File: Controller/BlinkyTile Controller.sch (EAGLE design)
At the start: 26 parts, among them CON1 USB_MICROSMT+THRUHULE, CON2 F-2X04-DIL-100, Q1 CRYSTAL_4PAD2520, SW1 SPST_TACT-EVQQ2, SW2 SPST_TACT-EVQQ2, U1 MK20D--VFM5, U2 W25Q80BV, U3 74LVC1G17DCK, U4 74LVC1G17DCK, U5 74LVC1G17DCK

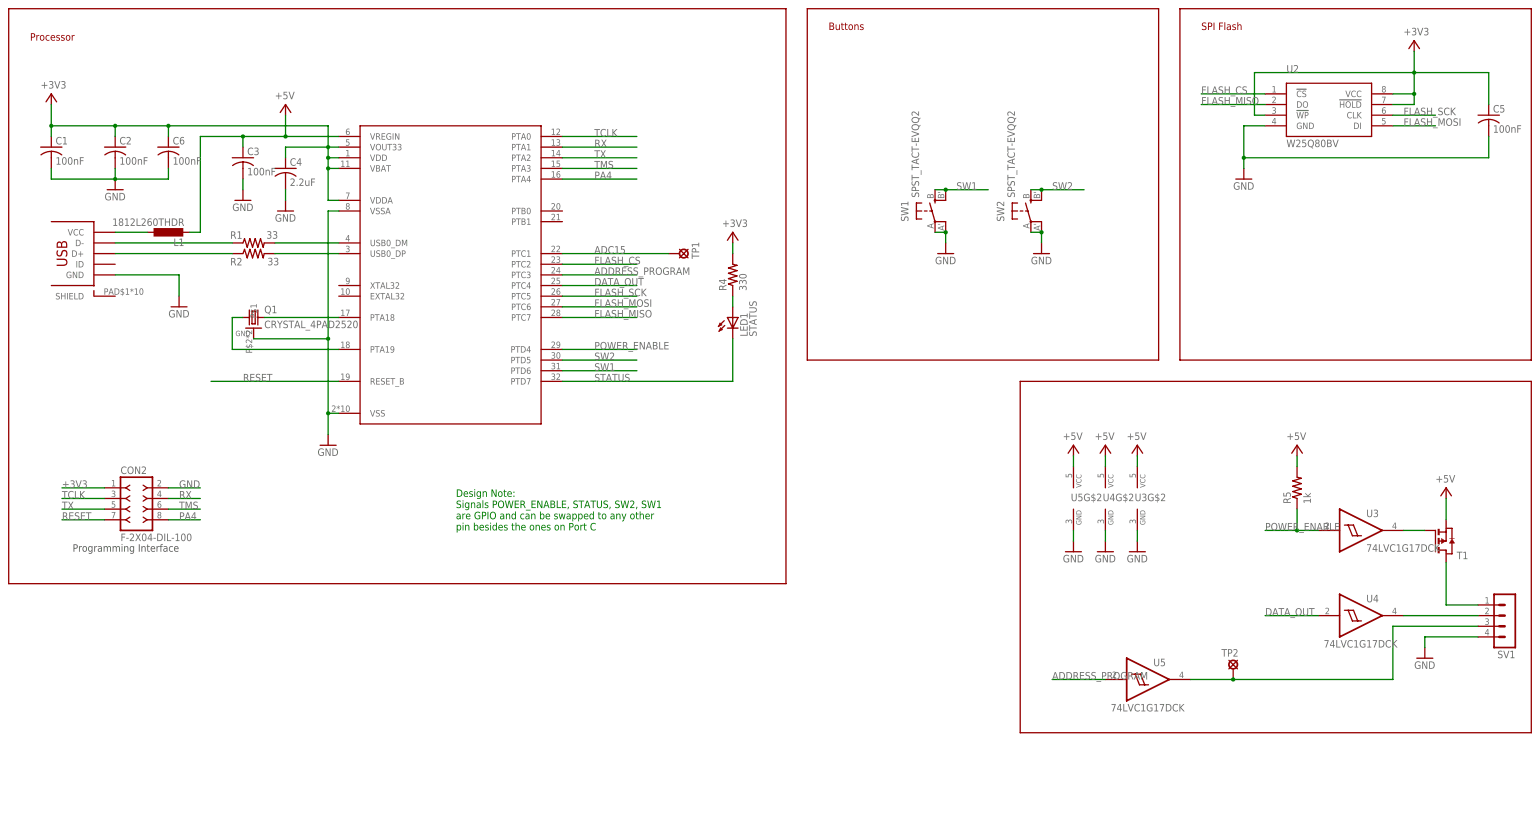
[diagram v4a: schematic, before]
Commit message: Updated controller and panel designs
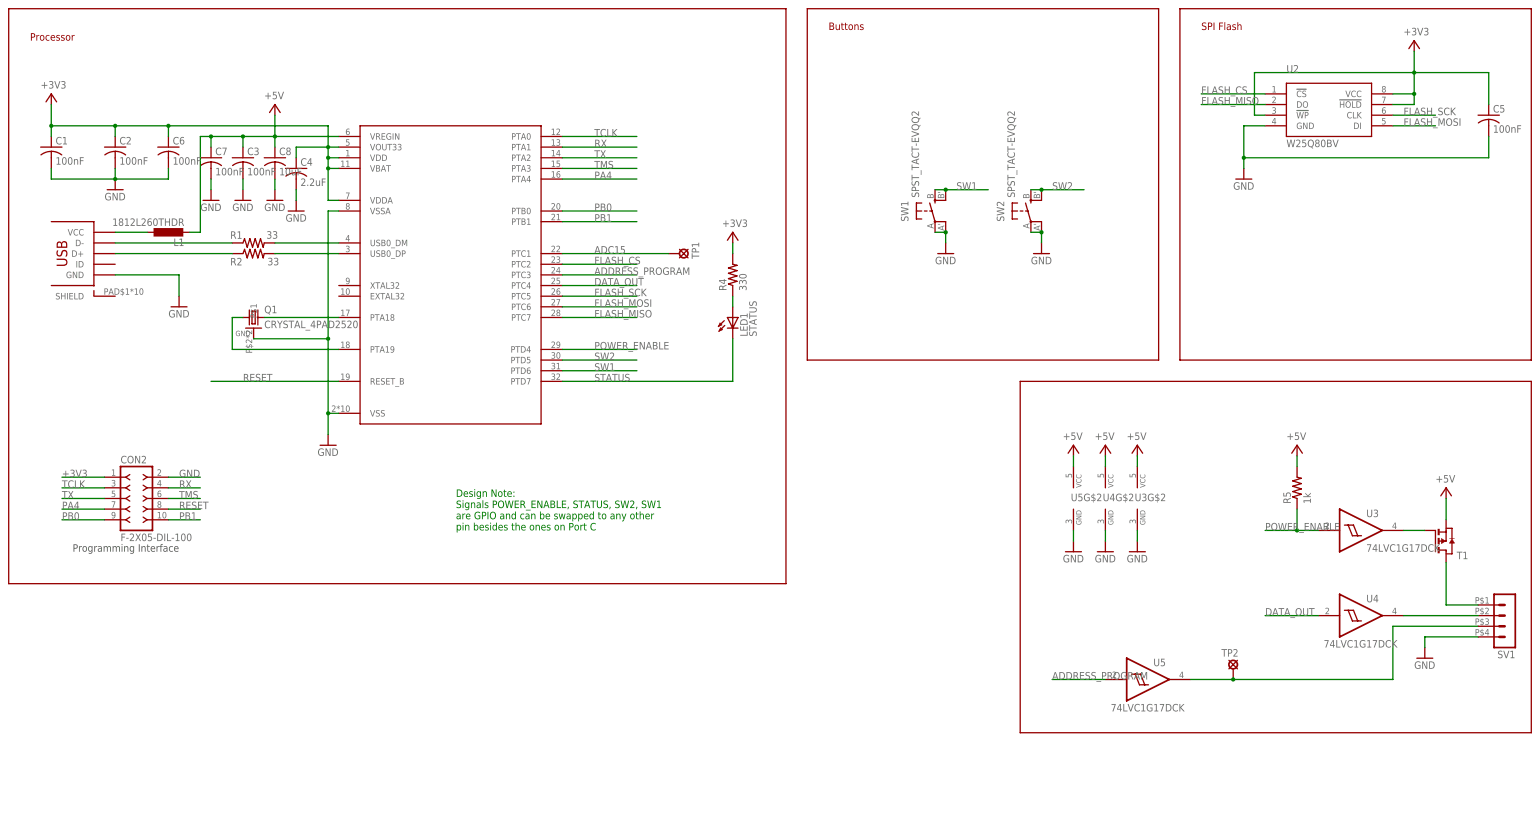
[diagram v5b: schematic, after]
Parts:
- added C7: 100nF, adafruit:C-USC0402
- added C8: 10uF, adafruit:C-USC0805K
- CON2: value F-2X04-DIL-100 -> F-2X05-DIL-100; device con-headers-jp:F-2X04-DIL-100 -> con-headers-jp:F-2X05-DIL-100
- SV1: device con-lstb:MA04-1 -> dodocohedreled:4-PIN_DUPONT
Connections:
- new net PB0: CON2.9, U1.PTB0
- new net PB1: CON2.10, U1.PTB1
- net +5V: now also C7.1, C8.1
- net GND: now also C7.2, C8.2
- net PA4: now also CON2.7; no longer CON2.8
- net RESET: now also CON2.8; no longer CON2.7
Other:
- moved on the sheet: C4, SV1
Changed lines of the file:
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@@
 <part name="TP2" library="solpad" deviceset="SE11" device="" value="ADDRESS"/>
 <part name="TP1" library="solpad" deviceset="SE11" device="" value="ADCIN"/>
-<part name="CON2" library="con-headers-jp" deviceset="F-2X04-" device="DIL-100" value="F-2X04-DIL-100"/>
+<part name="CON2" library="con-headers-jp" deviceset="F-2X05-" device="DIL-100" value="F-2X05-DIL-100"/>
 <part name="U3" library="74xx-little-us" deviceset="74*1G17" device="DCK" technology="LVC"/>
 <part name="T1" library="zetex" deviceset="PMOSSOT23" device=""/>
@@
 <part name="C6" library="adafruit" deviceset="C-US" device="C0402" value="100nF"/>
 <part name="R5" library="adafruit" deviceset="R-US_" device="R0402" value="1k"/>
+<part name="SV1" library="dodocohedreled" deviceset="4-PIN_DUPONT" device=""/>
 <part name="P+5" library="supply1" deviceset="+5V" device=""/>
-<part name="SV1" library="con-lstb" deviceset="MA04-1" device=""/>
+<part name="C7" library="adafruit" deviceset="C-US" device="C0402" value="100nF"/>
+<part name="GND6" library="supply1" deviceset="GND" device=""/>
+<part name="C8" library="adafruit" deviceset="C-US" device="C0805K" value="10uF"/>
+<part name="GND11" library="supply1" deviceset="GND" device=""/>
 </parts>
 <sheets>
@@
 <instance part="CON1" gate="G$1" x="33.02" y="190.5"/>
 <instance part="Q1" gate="G$1" x="73.66" y="175.26"/>
-<instance part="C4" gate="G$1" x="81.28" y="210.82"/>
-<instance part="GND9" gate="1" x="81.28" y="200.66"/>
+<instance part="C4" gate="G$1" x="83.82" y="210.82"/>
+<instance part="GND9" gate="1" x="83.82" y="200.66"/>
 <instance part="GND15" gate="1" x="40.64" y="205.74"/>
 <instance part="GND10" gate="1" x="309.88" y="208.28"/>
@@
 <attribute name="VALUE" x="185.42" y="196.85" size="1.778" layer="96"/>
 </instance>
-<instance part="P+9" gate="1" x="81.28" y="226.06" smashed="yes">
-<attribute name="VALUE" x="78.74" y="227.33" size="1.778" layer="96"/>
+<instance part="P+9" gate="1" x="78.74" y="226.06" smashed="yes">
+<attribute name="VALUE" x="76.2" y="227.33" size="1.778" layer="96"/>
 </instance>
 <instance part="C3" gate="G$1" x="71.12" y="213.36"/>
@@
 <instance part="C6" gate="G$1" x="53.34" y="215.9"/>
 <instance part="R5" gate="G$1" x="322.58" y="134.62" rot="R90"/>
+<instance part="SV1" gate="1" x="373.38" y="101.6" rot="R180"/>
 <instance part="P+5" gate="1" x="322.58" y="144.78" smashed="yes">
 <attribute name="VALUE" x="320.04" y="146.05" size="1.778" layer="96"/>
 </instance>
-<instance part="SV1" gate="1" x="373.38" y="101.6" rot="R180"/>
+<instance part="C7" gate="G$1" x="63.5" y="213.36"/>
+<instance part="GND6" gate="1" x="63.5" y="203.2"/>
+<instance part="C8" gate="G$1" x="78.74" y="213.36"/>
+<instance part="GND11" gate="1" x="78.74" y="203.2"/>
 </instances>
 <busses>
@@
 <segment>
 <pinref part="C4" gate="G$1" pin="2"/>
-<wire x1="81.28" y1="205.74" x2="81.28" y2="203.2" width="0.1524" layer="91"/>
+<wire x1="83.82" y1="205.74" x2="83.82" y2="203.2" width="0.1524" layer="91"/>
 <pinref part="GND9" gate="1" pin="GND"/>
 </segment>
@@
 <segment>
 <pinref part="CON2" gate="G$1" pin="2"/>
-<wire x1="53.34" y1="134.62" x2="60.96" y2="134.62" width="0.1524" layer="91"/>
-<label x="55.88" y="134.62" size="1.778" layer="95"/>
+<wire x1="53.34" y1="137.16" x2="60.96" y2="137.16" width="0.1524" layer="91"/>
+<label x="55.88" y="137.16" size="1.778" layer="95"/>
 </segment>
 <segment>
@@
 <junction x="91.44" y="170.18"/>
 </segment>
+<segment>
+<pinref part="C7" gate="G$1" pin="2"/>
+<pinref part="GND6" gate="1" pin="GND"/>
+<wire x1="63.5" y1="208.28" x2="63.5" y2="205.74" width="0.1524" layer="91"/>
+</segment>
+<segment>
+<pinref part="C8" gate="G$1" pin="2"/>
+<pinref part="GND11" gate="1" pin="GND"/>
+<wire x1="78.74" y1="208.28" x2="78.74" y2="205.74" width="0.1524" layer="91"/>
+</segment>
 </net>
 <net name="N$2" class="0">
@@
 <wire x1="60.96" y1="195.58" x2="60.96" y2="218.44" width="0.1524" layer="91"/>
 <pinref part="U1" gate="G$1" pin="VREGIN"/>
-<wire x1="93.98" y1="218.44" x2="81.28" y2="218.44" width="0.1524" layer="91"/>
-<wire x1="81.28" y1="223.52" x2="81.28" y2="218.44" width="0.1524" layer="91"/>
-<junction x="81.28" y="218.44"/>
+<wire x1="93.98" y1="218.44" x2="78.74" y2="218.44" width="0.1524" layer="91"/>
+<wire x1="78.74" y1="223.52" x2="78.74" y2="218.44" width="0.1524" layer="91"/>
+<junction x="78.74" y="218.44"/>
 <pinref part="C3" gate="G$1" pin="1"/>
-<wire x1="71.12" y1="218.44" x2="60.96" y2="218.44" width="0.1524" layer="91"/>
+<wire x1="71.12" y1="218.44" x2="63.5" y2="218.44" width="0.1524" layer="91"/>
+<wire x1="63.5" y1="218.44" x2="60.96" y2="218.44" width="0.1524" layer="91"/>
 <wire x1="71.12" y1="218.44" x2="71.12" y2="215.9" width="0.1524" layer="91"/>
-<wire x1="81.28" y1="218.44" x2="71.12" y2="218.44" width="0.1524" layer="91"/>
+<wire x1="78.74" y1="218.44" x2="71.12" y2="218.44" width="0.1524" layer="91"/>
 <junction x="71.12" y="218.44"/>
+<pinref part="C7" gate="G$1" pin="1"/>
+<wire x1="63.5" y1="215.9" x2="63.5" y2="218.44" width="0.1524" layer="91"/>
+<junction x="63.5" y="218.44"/>
+<pinref part="C8" gate="G$1" pin="1"/>
+<wire x1="78.74" y1="215.9" x2="78.74" y2="218.44" width="0.1524" layer="91"/>
 </segment>
 <segment>
@@
 <segment>
 <pinref part="R5" gate="G$1" pin="2"/>
+<wire x1="322.58" y1="142.24" x2="322.58" y2="139.7" width="0.1524" layer="91"/>
 <pinref part="P+5" gate="1" pin="+5V"/>
-<wire x1="322.58" y1="142.24" x2="322.58" y2="139.7" width="0.1524" layer="91"/>
 </segment>
 </net>
@@
 <pinref part="U1" gate="G$1" pin="VBAT"/>
 <pinref part="C4" gate="G$1" pin="1"/>
-<wire x1="81.28" y1="215.9" x2="81.28" y2="213.36" width="0.1524" layer="91"/>
+<wire x1="83.82" y1="215.9" x2="83.82" y2="213.36" width="0.1524" layer="91"/>
 <pinref part="U1" gate="G$1" pin="VOUT33"/>
 <wire x1="93.98" y1="215.9" x2="91.44" y2="215.9" width="0.1524" layer="91"/>
-<wire x1="91.44" y1="215.9" x2="81.28" y2="215.9" width="0.1524" layer="91"/>
+<wire x1="91.44" y1="215.9" x2="83.82" y2="215.9" width="0.1524" layer="91"/>
 <wire x1="91.44" y1="215.9" x2="91.44" y2="213.36" width="0.1524" layer="91"/>
 <pinref part="U1" gate="G$1" pin="VDD"/>
@@
 <segment>
 <pinref part="CON2" gate="G$1" pin="1"/>
+<wire x1="38.1" y1="137.16" x2="27.94" y2="137.16" width="0.1524" layer="91"/>
+<label x="27.94" y="137.16" size="1.778" layer="95"/>
+</segment>
+</net>
+<net name="TCLK" class="0">
+<segment>
+<pinref part="CON2" gate="G$1" pin="3"/>
 <wire x1="38.1" y1="134.62" x2="27.94" y2="134.62" width="0.1524" layer="91"/>
 <label x="27.94" y="134.62" size="1.778" layer="95"/>
-</segment>
-</net>
-<net name="TCLK" class="0">
-<segment>
-<pinref part="CON2" gate="G$1" pin="3"/>
-<wire x1="38.1" y1="132.08" x2="27.94" y2="132.08" width="0.1524" layer="91"/>
-<label x="27.94" y="132.08" size="1.778" layer="95"/>
 </segment>
 <segment>
@@
 <segment>
 <pinref part="CON2" gate="G$1" pin="6"/>
-<wire x1="53.34" y1="129.54" x2="60.96" y2="129.54" width="0.1524" layer="91"/>
-<label x="55.88" y="129.54" size="1.778" layer="95"/>
+<wire x1="53.34" y1="132.08" x2="60.96" y2="132.08" width="0.1524" layer="91"/>
+<label x="55.88" y="132.08" size="1.778" layer="95"/>
 </segment>
 </net>
@@
 <segment>
 <pinref part="CON2" gate="G$1" pin="4"/>
-<wire x1="60.96" y1="132.08" x2="53.34" y2="132.08" width="0.1524" layer="91"/>
-<label x="55.88" y="132.08" size="1.778" layer="95"/>
+<wire x1="60.96" y1="134.62" x2="53.34" y2="134.62" width="0.1524" layer="91"/>
+<label x="55.88" y="134.62" size="1.778" layer="95"/>
 </segment>
 </net>
@@
 <segment>
 <pinref part="CON2" gate="G$1" pin="5"/>
-<wire x1="38.1" y1="129.54" x2="27.94" y2="129.54" width="0.1524" layer="91"/>
-<label x="27.94" y="129.54" size="1.778" layer="95"/>
+<wire x1="38.1" y1="132.08" x2="27.94" y2="132.08" width="0.1524" layer="91"/>
+<label x="27.94" y="132.08" size="1.778" layer="95"/>
 </segment>
 </net>
@@
 </segment>
 <segment>
-<pinref part="CON2" gate="G$1" pin="7"/>
-<wire x1="38.1" y1="127" x2="27.94" y2="127" width="0.1524" layer="91"/>
-<label x="27.94" y="127" size="1.778" layer="95"/>
+<pinref part="CON2" gate="G$1" pin="8"/>
+<wire x1="53.34" y1="129.54" x2="60.96" y2="129.54" width="0.1524" layer="91"/>
+<label x="55.88" y="129.54" size="1.778" layer="95"/>
 </segment>
 </net>
@@
 </segment>
 <segment>
-<pinref part="CON2" gate="G$1" pin="8"/>
+<pinref part="CON2" gate="G$1" pin="7"/>
+<wire x1="38.1" y1="129.54" x2="27.94" y2="129.54" width="0.1524" layer="91"/>
+<label x="27.94" y="129.54" size="1.778" layer="95"/>
+</segment>
+</net>
+<net name="PB0" class="0">
+<segment>
+<pinref part="U1" gate="G$1" pin="PTB0"/>
+<wire x1="147.32" y1="200.66" x2="165.1" y2="200.66" width="0.1524" layer="91"/>
+<label x="154.94" y="200.66" size="1.778" layer="95"/>
+</segment>
+<segment>
+<pinref part="CON2" gate="G$1" pin="9"/>
+<wire x1="38.1" y1="127" x2="27.94" y2="127" width="0.1524" layer="91"/>
+<label x="27.94" y="127" size="1.778" layer="95"/>
+</segment>
+</net>
+<net name="PB1" class="0">
+<segment>
+<pinref part="U1" gate="G$1" pin="PTB1"/>
+<wire x1="147.32" y1="198.12" x2="165.1" y2="198.12" width="0.1524" layer="91"/>
+<label x="154.94" y="198.12" size="1.778" layer="95"/>
+</segment>
+<segment>
+<pinref part="CON2" gate="G$1" pin="10"/>
 <wire x1="53.34" y1="127" x2="60.96" y2="127" width="0.1524" layer="91"/>
 <label x="55.88" y="127" size="1.778" layer="95"/>

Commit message: Updated controller board, by Sam
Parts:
- removed C7: 100nF, adafruit:C-USC0402
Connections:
- net +5V: no longer C7.1
- net GND: no longer C7.2
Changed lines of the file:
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@@
 <part name="SV1" library="dodocohedreled" deviceset="4-PIN_DUPONT" device=""/>
 <part name="P+5" library="supply1" deviceset="+5V" device=""/>
-<part name="C7" library="adafruit" deviceset="C-US" device="C0402" value="100nF"/>
-<part name="GND6" library="supply1" deviceset="GND" device=""/>
 <part name="C8" library="adafruit" deviceset="C-US" device="C0805K" value="10uF"/>
 <part name="GND11" library="supply1" deviceset="GND" device=""/>
@@
 <attribute name="VALUE" x="320.04" y="146.05" size="1.778" layer="96"/>
 </instance>
-<instance part="C7" gate="G$1" x="63.5" y="213.36"/>
-<instance part="GND6" gate="1" x="63.5" y="203.2"/>
 <instance part="C8" gate="G$1" x="78.74" y="213.36"/>
 <instance part="GND11" gate="1" x="78.74" y="203.2"/>
@@
 </segment>
 <segment>
-<pinref part="C7" gate="G$1" pin="2"/>
-<pinref part="GND6" gate="1" pin="GND"/>
-<wire x1="63.5" y1="208.28" x2="63.5" y2="205.74" width="0.1524" layer="91"/>
-</segment>
-<segment>
 <pinref part="C8" gate="G$1" pin="2"/>
 <pinref part="GND11" gate="1" pin="GND"/>
@@
 <junction x="78.74" y="218.44"/>
 <pinref part="C3" gate="G$1" pin="1"/>
-<wire x1="71.12" y1="218.44" x2="63.5" y2="218.44" width="0.1524" layer="91"/>
-<wire x1="63.5" y1="218.44" x2="60.96" y2="218.44" width="0.1524" layer="91"/>
+<wire x1="71.12" y1="218.44" x2="60.96" y2="218.44" width="0.1524" layer="91"/>
 <wire x1="71.12" y1="218.44" x2="71.12" y2="215.9" width="0.1524" layer="91"/>
 <wire x1="78.74" y1="218.44" x2="71.12" y2="218.44" width="0.1524" layer="91"/>
 <junction x="71.12" y="218.44"/>
-<pinref part="C7" gate="G$1" pin="1"/>
-<wire x1="63.5" y1="215.9" x2="63.5" y2="218.44" width="0.1524" layer="91"/>
-<junction x="63.5" y="218.44"/>
 <pinref part="C8" gate="G$1" pin="1"/>
 <wire x1="78.74" y1="215.9" x2="78.74" y2="218.44" width="0.1524" layer="91"/>
